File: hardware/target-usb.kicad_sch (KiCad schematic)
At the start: 23 parts, among them IC3 MAX9032AKA+T, IC4 USB3343, IC5 MAX9032AKA+T, IC6 DSC6101CI2A-026.0000, IC7 MAX9032AKA+T

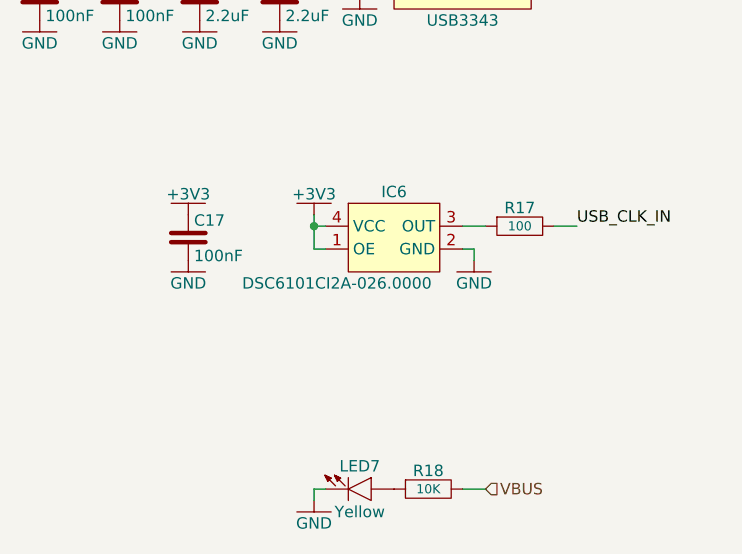
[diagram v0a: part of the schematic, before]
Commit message: replace obsolete components, updated PCB, schematics and production files
Signed-off-by: Jakub Sobota <jakub.sobota@3mdeb.com>
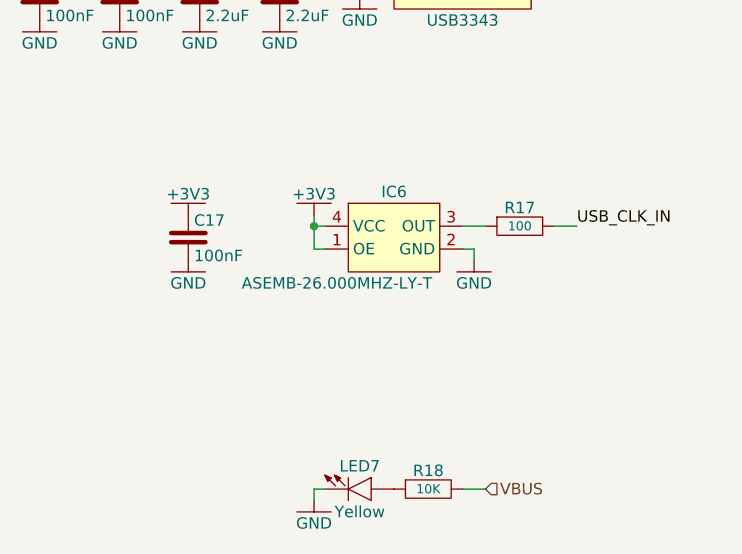
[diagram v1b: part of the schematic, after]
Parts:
- IC6: value DSC6101CI2A-026.0000 -> ASEMB-26.000MHZ-LY-T
